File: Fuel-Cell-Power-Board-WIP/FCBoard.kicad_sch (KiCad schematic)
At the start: 99 parts, among them J1 STD_PWR_HEADER, J2 DE9_Receptacle, J3 STD_PWR_HEADER, J4 STD_PWR_HEADER, J5 Conn_02x05_Odd_Even, J6 STD_PWR_HEADER, J7 DA15_Receptacle_MountingHoles, J7 USB_B_Micro, Q1 NMOS, SW1 PTS815 SJM 250 SMTR LFS, SW2 PTS815 SJM 250 SMTR LFS, U2 LM2576D2TR4-5G, U3 RPA60-2412SFW, U3 TPS2596, U4 STM32L432KCUx, U6 FT234XD-R, U7 LD39050PU33R, U9 MCP2542FD-E/SN, U9 USBLC6-2SC6, X1 OXETDLJANF-8MHZ

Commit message: Began PCB layout.
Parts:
- C4: footprint (none) -> FPCB_Footprints:PCAP_10x10-ELECT_NCA
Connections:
- net +12V is gone; now on net 12V_{FC}: C1.1, U2.1 (VIN)
- net I_{MON}: no longer R9.1, U3.7 (ILM)
- net ~{FAULT}: no longer Q1.2 (G), R10.2, U3.6 (~{FAULT})
- new net I_{MON}12V: R9.1, U3.7 (ILM)
- new net ~{FAULT}12V: Q1.2 (G), R10.2, U3.6 (~{FAULT})
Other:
- note added: "Fuel Cell Power In and 12V DCDC"
- moved on the sheet: J3, J4

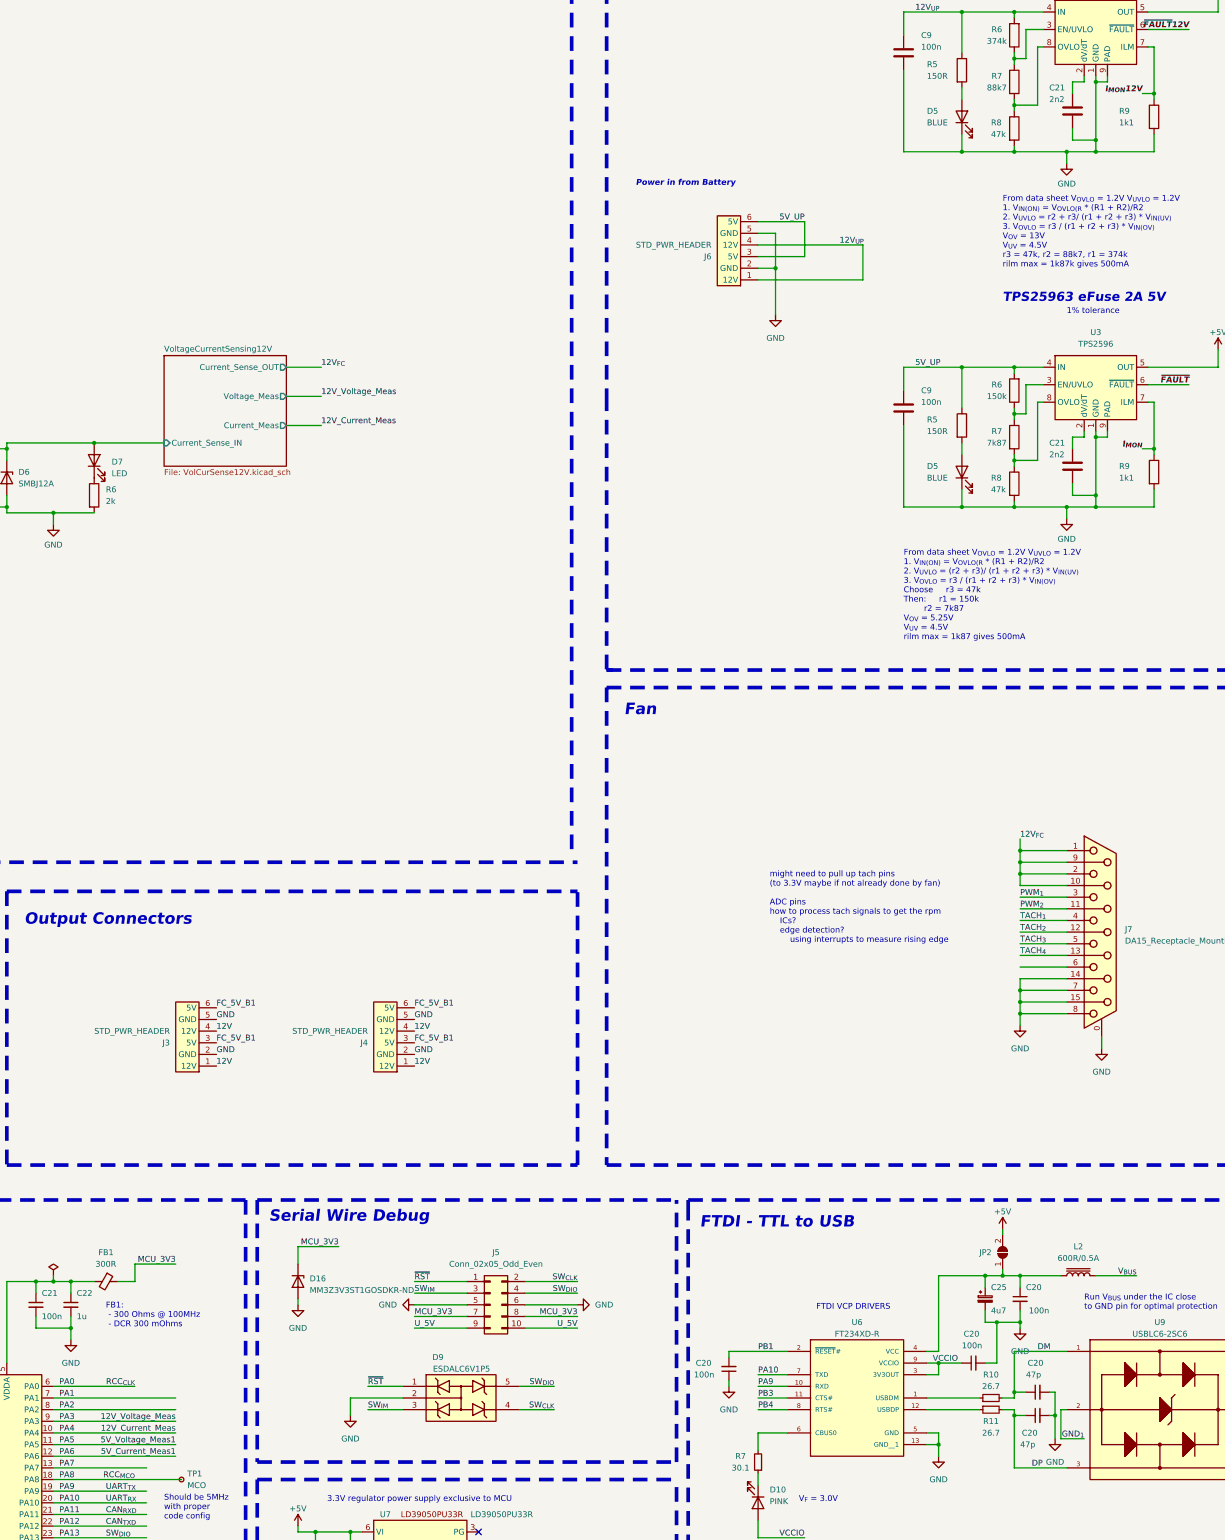
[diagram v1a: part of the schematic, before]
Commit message: Routed PCB except for battery 5V
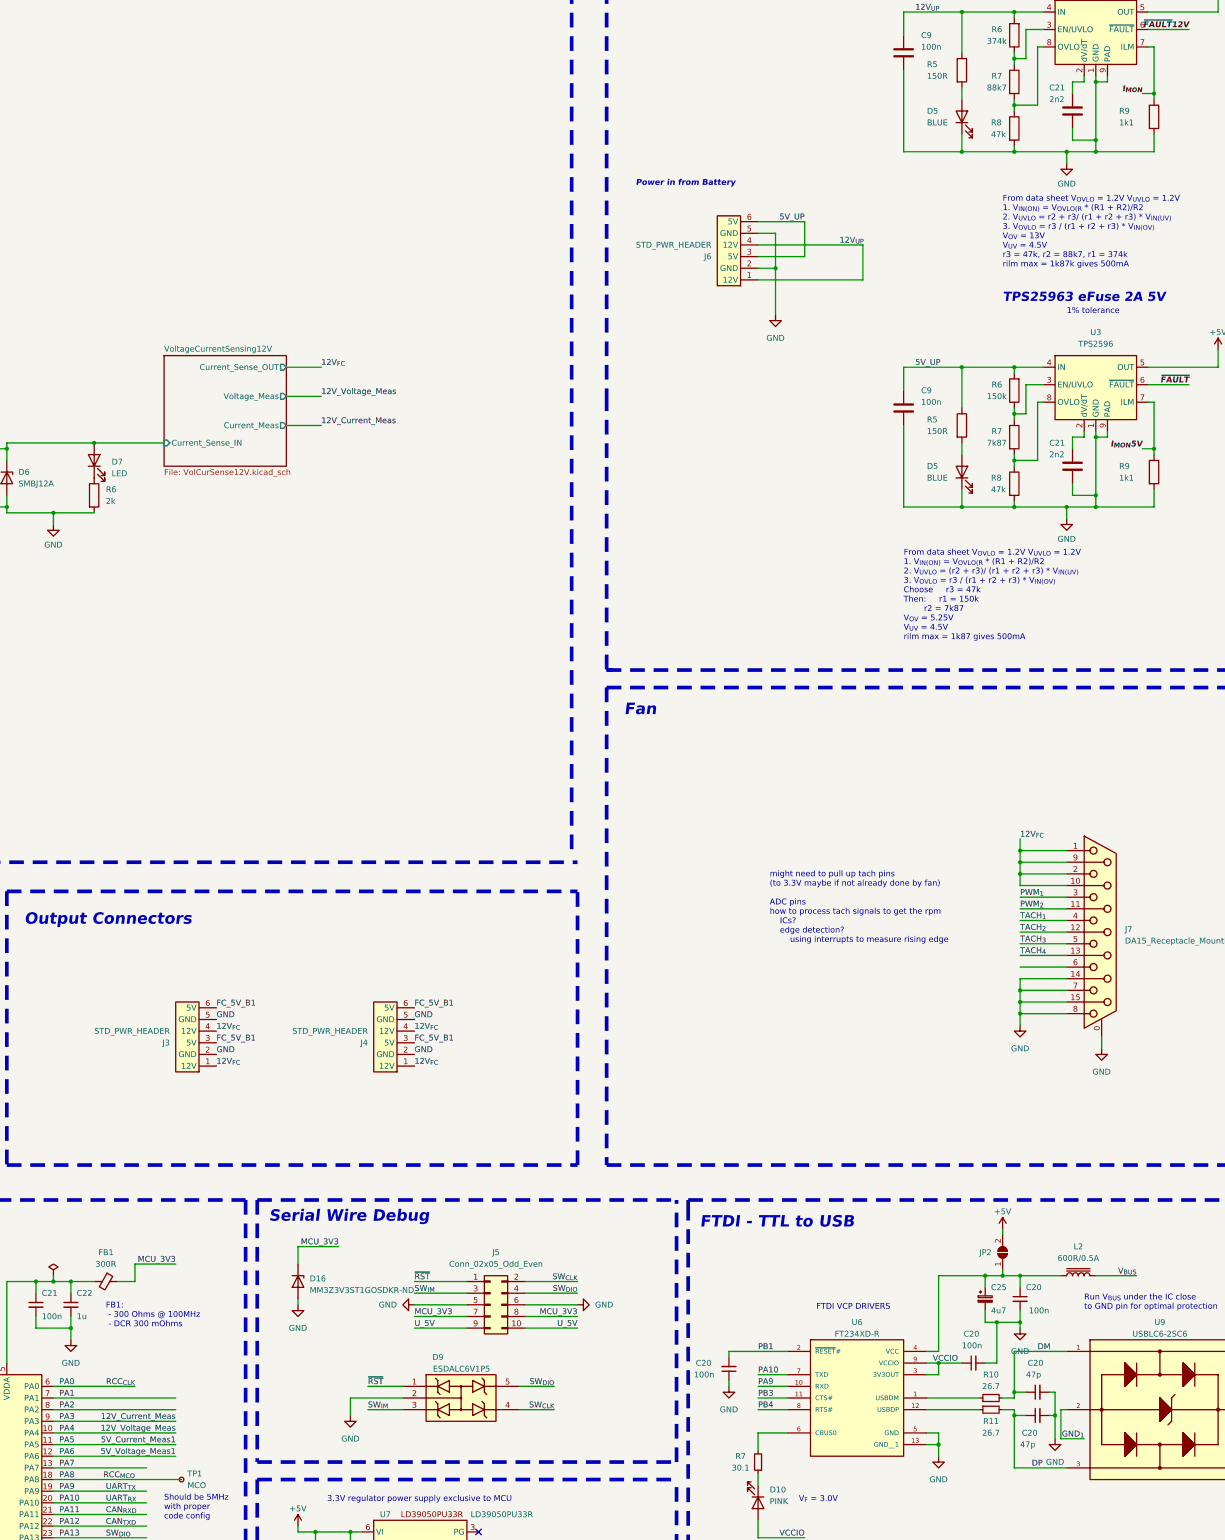
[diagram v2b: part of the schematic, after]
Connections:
- net 12V is gone; now on net 12V_{FC}: J3.1 (12V), J3.4 (12V), J4.1 (12V), J4.4 (12V)
- net I_{MON}12V is gone; now on net I_{MON}: R9.1, U3.7 (ILM)
- net 12V_Current_Meas: now also U4.9 (PA3); no longer U4.10 (PA4)
- net 12V_Voltage_Meas: now also U4.10 (PA4); no longer U4.9 (PA3)
- net 5V_Current_Meas1: now also U4.11 (PA5); no longer U4.12 (PA6)
- net 5V_Voltage_Meas1: now also U4.12 (PA6); no longer U4.11 (PA5)
- net I_{MON}: no longer R9.1, U3.7 (ILM)
- new net I_{MON}5V: R9.1, U3.7 (ILM)
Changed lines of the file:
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@@
-    (effects (font (size 1.27 1.27)) (justify left bottom))
-  )
-  (label "12V" (at 303.53 267.97 0) (fields_autoplaced)
     (effects (font (size 1.27 1.27)) (justify left bottom))
   )
@@
     (effects (font (size 1.27 1.27)) (justify left bottom))
   )
+  (label "12V_{FC}" (at 303.53 267.97 0) (fields_autoplaced)
+    (effects (font (size 1.27 1.27)) (justify left bottom))
+  )
   (label "~{FAULT}12V" (at 535.94 68.58 180) (fields_autoplaced)
     (effects (font (size 1.27 1.27) bold italic) (justify right bottom))
@@
     (effects (font (size 1.27 1.27) bold italic) (justify right bottom))
   )
-  (label "12V_Current_Meas" (at 294.64 347.98 180) (fields_autoplaced)
-    (effects (font (size 1.27 1.27)) (justify right bottom))
+  (label "5V_Current_Meas1" (at 294.64 350.52 180) (fields_autoplaced)
+    (effects (font (size 1.27 1.27)) (justify right bottom))
+  )
+  (label "12V_{FC}" (at 346.71 260.35 0) (fields_autoplaced)
+    (effects (font (size 1.27 1.27)) (justify left bottom))
   )
   (label "12V_{FC}" (at 326.39 115.57 0) (fields_autoplaced)
@@
     (effects (font (size 1.27 1.27)) (justify left bottom))
   )
-  (label "12V" (at 346.71 267.97 0) (fields_autoplaced)
-    (effects (font (size 1.27 1.27)) (justify left bottom))
-  )
   (label "PA11" (at 269.24 365.76 0) (fields_autoplaced)
     (effects (font (size 1.27 1.27)) (justify left bottom))
@@
     (effects (font (size 1.27 1.27)) (justify left bottom))
   )
-  (label "12V" (at 303.53 260.35 0) (fields_autoplaced)
-    (effects (font (size 1.27 1.27)) (justify left bottom))
-  )
   (label "V_{BUS}" (at 504.19 313.69 180) (fields_autoplaced)
     (effects (font (size 1.27 1.27)) (justify right bottom))
@@
     (effects (font (size 1.27 1.27)) (justify left bottom))
   )
-  (label "12V_Voltage_Meas" (at 294.64 345.44 180) (fields_autoplaced)
-    (effects (font (size 1.27 1.27)) (justify right bottom))
-  )
   (label "PB3" (at 237.49 360.68 0) (fields_autoplaced)
     (effects (font (size 1.27 1.27)) (justify left bottom))
@@
     (effects (font (size 1.27 1.27)) (justify left bottom))
   )
-  (label "12V" (at 346.71 260.35 0) (fields_autoplaced)
-    (effects (font (size 1.27 1.27)) (justify left bottom))
+  (label "12V_Current_Meas" (at 294.64 345.44 180) (fields_autoplaced)
+    (effects (font (size 1.27 1.27)) (justify right bottom))
   )
   (label "SW_{IM}" (at 346.71 317.5 0) (fields_autoplaced)
@@
     (effects (font (size 1.27 1.27)) (justify right bottom))
   )
-  (label "5V_Voltage_Meas1" (at 294.64 350.52 180) (fields_autoplaced)
-    (effects (font (size 1.27 1.27)) (justify right bottom))
-  )
   (label "12V_{FC}" (at 30.48 252.73 0) (fields_autoplaced)
     (effects (font (size 1.27 1.27)) (justify left bottom))
@@
     (effects (font (size 1.27 1.27)) (justify left bottom))
   )
+  (label "5V_Voltage_Meas1" (at 294.64 353.06 180) (fields_autoplaced)
+    (effects (font (size 1.27 1.27)) (justify right bottom))
+  )
   (label "U_5V" (at 346.71 325.12 0) (fields_autoplaced)
     (effects (font (size 1.27 1.27)) (justify left bottom))
@@
     (effects (font (size 1.27 1.27)) (justify left bottom))
   )
-  (label "5V_Current_Meas1" (at 294.64 353.06 180) (fields_autoplaced)
-    (effects (font (size 1.27 1.27)) (justify right bottom))
-  )
   (label "PB0" (at 237.49 355.6 0) (fields_autoplaced)
     (effects (font (size 1.27 1.27)) (justify left bottom))
@@
     (effects (font (size 1.27 1.27)) (justify left bottom))
   )
-  (label "I_{MON}12V" (at 505.46 55.88 180) (fields_autoplaced)
+  (label "I_{MON}" (at 505.46 55.88 180) (fields_autoplaced)
     (effects (font (size 1.27 1.27) bold italic) (justify right bottom))
   )
@@
     (effects (font (size 1.27 1.27)) (justify left bottom))
   )
-  (label "I_{MON}" (at 505.46 133.35 180) (fields_autoplaced)
+  (label "I_{MON}5V" (at 505.46 133.35 180) (fields_autoplaced)
     (effects (font (size 1.27 1.27) bold italic) (justify right bottom))
   )
@@
     (effects (font (size 1.27 1.27)) (justify left bottom))
   )
+  (label "12V_Voltage_Meas" (at 294.64 347.98 180) (fields_autoplaced)
+    (effects (font (size 1.27 1.27)) (justify right bottom))
+  )
   (label "GND" (at 303.53 265.43 0) (fields_autoplaced)
     (effects (font (size 1.27 1.27)) (justify left bottom))
@@
     (effects (font (size 1.27 1.27)) (justify left bottom))
   )
+  (label "12V_{FC}" (at 346.71 267.97 0) (fields_autoplaced)
+    (effects (font (size 1.27 1.27)) (justify left bottom))
+  )
   (label "GND_{1}" (at 554.99 353.06 0) (fields_autoplaced)
     (effects (font (size 1.27 1.27)) (justify left bottom))
@@
     (effects (font (size 1.27 1.27)) (justify left bottom))
   )
+  (label "12V_{FC}" (at 303.53 260.35 0) (fields_autoplaced)
+    (effects (font (size 1.27 1.27)) (justify left bottom))
+  )

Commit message: moved james pcb to another folder so we can do rev 2 of the layout, changed some footprints to be consistent with kicad, changed the inductor to a smaller bit similar package with certain characteristics
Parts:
- removed C11: 100u, FPCB_Footprints:CAP_UAQ_12P5X20_NCH, symbol Device:C_Polarized
- added C12: 100u, Capacitor_THT:CP_Radial_D12.5mm_P5.00mm, symbol Device:C_Polarized
- added L1: 100u, FPCB_Footprints:IND_101M51_VIS, symbol Device:L
- C4: footprint FPCB_Footprints:PCAP_10x10-ELECT_NCA -> Capacitor_SMD:CP_Elec_10x10
- C5: footprint FPCB_Footprints:CAP_UAQ_12P5X20_NCH -> Capacitor_THT:CP_Radial_D12.5mm_P5.00mm
- L2: renamed from L1; footprint FPCB_Footprints:IND_101M51_VIS -> Inductor_SMD:L_Vishay_IHLP-6767; Name IHLP8787MZER101M51 -> 541-1294-1-ND
- R2: value 3.1k -> 0R
- R3: now not fitted
- renumbered C6 to C8, D2 to D1, D1 to D2, L2 to L3
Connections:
- net GND: now also C12.2
- net VoltageCurrentSensing12V/Current_Sense_IN: now also C12.1

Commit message: updated schematic slightly
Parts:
- added C22: 1u, Capacitor_SMD:C_0603_1608Metric, symbol Device:C_Small
- added R10 (x2): 10k, Resistor_SMD:R_0603_1608Metric, symbol Device:R
- added U14: TSV912IDT, symbol Amplifier_Operational:TSV912IDT
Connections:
- net TACH_{1} is gone; now on net PA1: J7.4
- net TACH_{2} is gone; now on net PA2: J7.12 (P12)
- net +5V: now also C22.1, U14.8 (V+)
- net GND: now also C22.2, U14.4 (V-)
- net MCU_3V3: now also R10.1, R10.1
- net PA1: now also R10.2
- net PA2: now also R10.2
- net PB5: now also U14.3 (+)
- net PB6: now also U14.5 (+)
- net PWM_{1}: no longer names the net of J7.3
- net PWM_{1}: now also U14.1, U14.2 (-)
- net PWM_{2}: no longer names the net of J7.11 (P111)
- net PWM_{2}: now also U14.6 (-), U14.7
- no-connect marks 8 -> 20
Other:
- note added: "Positive pull up logic for CTRL pin, open circuit is on"
- moved on the sheet: J7

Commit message: started rework
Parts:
- removed C21: 2n2, Capacitor_SMD:C_0603_1608Metric, symbol Device:C
- removed C9: 100n, Capacitor_SMD:C_0603_1608Metric, symbol Device:C
- removed D5: BLUE, LED_SMD:LED_0603_1608Metric, symbol Device:LED
- removed D6: RED, LED_SMD:LED_0603_1608Metric, symbol Device:LED
- removed Q1 (x2): NMOS, Package_TO_SOT_SMD:SOT-523, symbol Simulation_SPICE:NMOS
- removed R10: 10k, Resistor_SMD:R_0603_1608Metric, symbol Device:R
- removed R11: 120R, Resistor_SMD:R_0603_1608Metric, symbol Device:R
- removed R5: 150R, Resistor_SMD:R_0603_1608Metric, symbol Device:R
- removed R6: 374k, Resistor_SMD:R_0603_1608Metric, symbol Device:R
- removed R7: 88k7, Resistor_SMD:R_0603_1608Metric, symbol Device:R
- removed R8: 47k, Resistor_SMD:R_0603_1608Metric, symbol Device:R
- removed R9: 1k1, Resistor_SMD:R_0603_1608Metric, symbol Device:R
- removed U3: TPS2596, Package_SO:TI_SO-PowerPAD-8, symbol H2_Parts:TPS2596
- added H1, H2, H3, H4: MountingHole, MountingHole:MountingHole_3.2mm_M3, symbol Mechanical:MountingHole
- added Q1: SI2302A-TPMSCT-ND, Package_TO_SOT_SMD:SOT-23-3, symbol Device:Q_NMOS_GSD
- C10, C9: footprint Capacitor_SMD:C_1812_4532Metric -> Capacitor_SMD:C_2220_5650Metric; Part 1812GC682KAT1A -> 478-5929-2-ND
- C22: value 1u -> 100n
- U7: renamed from U14; footprint (none) -> BATT_FTP:SO8_STM
- renumbered C25 to C24, R10 to R11, R11 to R12
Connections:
- net GND: now also Q1.2 (S)
- net ~{FAULT}: now also Q1.1 (G)
- net at D6.1 (K): now also Q1.3 (D)
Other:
- note removed: "From data sheet V_{OVLO} = 1.2V V_{UVLO} = 1.2V 1. V_{IN(ON)} = V_{OVLO(R} * (R1 + R2)/R2 2. V_{UVLO} = r2 + r3/ (r1 + r2 + r3) * V_{IN(UV)} 3. V_{OVLO} = r3 / (r1 + r2 + r3) * V_{IN(OV)} V_{OV} = 13V V_{UV} = 4.5V r3 = 47k, r2 = 88k7, r1 = 374k rilm max = 1k87k gives 500mA"
- note removed: "TPS25963 eFuse 2A 12V"

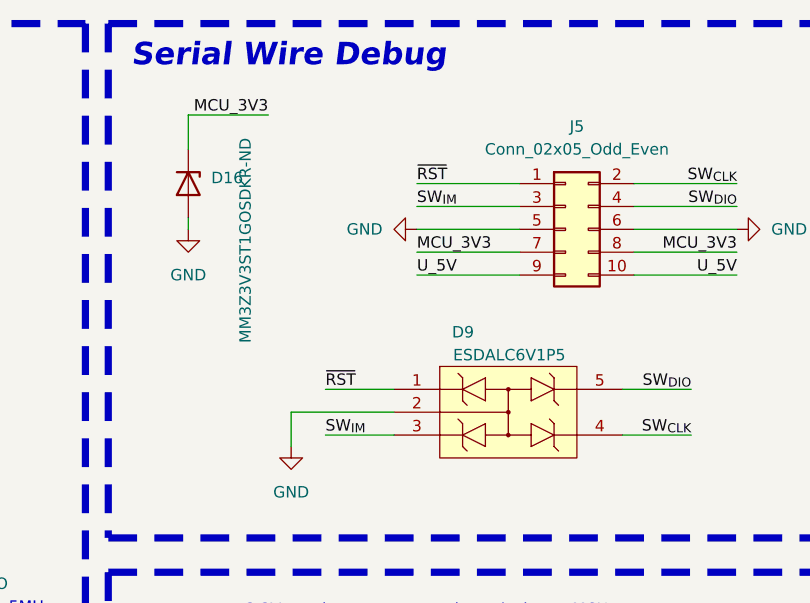
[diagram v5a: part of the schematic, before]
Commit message: Reworked mcu layout for caps, reworked ftdi chip layout, reworked lots of other things too
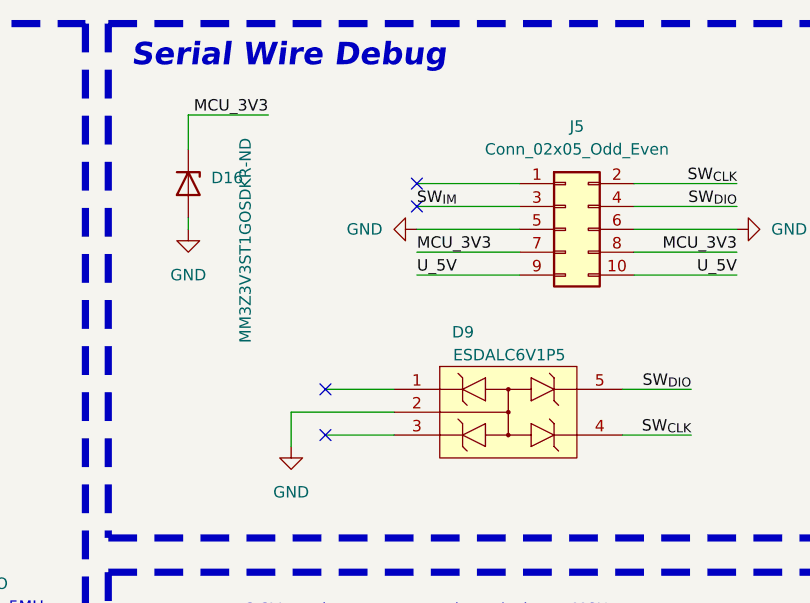
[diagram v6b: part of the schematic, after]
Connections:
- net SW_{IM}: no longer D9.3
- net ~{RST}: no longer D9.1, J5.1 (Pin_1)
- no-connect marks 20 -> 24
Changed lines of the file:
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@@
   (no_connect (at 505.46 245.11))
   (no_connect (at 226.06 138.43))
+  (no_connect (at 346.71 314.96))
   (no_connect (at 86.36 345.44))
+  (no_connect (at 336.55 337.82))
   (no_connect (at 109.22 332.74))
   (no_connect (at 505.46 250.19))
   (no_connect (at 86.36 337.82))
+  (no_connect (at 346.71 317.5))
+  (no_connect (at 336.55 342.9))
   (no_connect (at 237.49 350.52))
   (no_connect (at 86.36 330.2))
@@
     (effects (font (size 1.27 1.27)) (justify right bottom))
   )
-  (label "~{RST}" (at 336.55 337.82 0) (fields_autoplaced)
-    (effects (font (size 1.27 1.27)) (justify left bottom))
-  )
   (label "TACH_{2}" (at 505.46 242.57 0) (fields_autoplaced)
     (effects (font (size 1.27 1.27)) (justify left bottom))
@@
     (effects (font (size 1.27 1.27)) (justify left bottom))
   )
-  (label "SW_{IM}" (at 336.55 342.9 0) (fields_autoplaced)
-    (effects (font (size 1.27 1.27)) (justify left bottom))
-  )
   (label "V+" (at 101.6 330.2 0) (fields_autoplaced)
     (effects (font (size 1.27 1.27)) (justify left bottom))
@@
     (effects (font (size 1.27 1.27)) (justify left bottom))
   )
-  (label "~{RST}" (at 346.71 314.96 0) (fields_autoplaced)
-    (effects (font (size 1.27 1.27)) (justify left bottom))
-  )

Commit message: finished up pcb
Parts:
- removed L1: 100u, FPCB_Footprints:IND_101M51_VIS, symbol Device:L
- added JP3: SolderJumper_3_Open, Jumper:SolderJumper-3_P1.3mm_Open_RoundedPad1.0x1.5mm_NumberLabels, symbol Jumper:SolderJumper_3_Open
- added Q2, Q3: SI2302A-TPMSCT-ND, Package_TO_SOT_SMD:SOT-23-3, symbol Device:Q_NMOS_GSD
- added R10 (x2): 10k, Resistor_SMD:R_0603_1608Metric, symbol Device:R
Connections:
- net 12V_{FC}: now also JP3.1 (A)
- net GND: now also Q2.2 (S), Q3.2 (S)
- net MCU_3V3: now also JP3.3 (B)
- net at U7.1, U7.2 (-): now also Q3.1 (G); no longer J7.3
- net at U7.6 (-), U7.7: now also Q2.1 (G); no longer J7.11 (P111)
- new net: JP3.2 (C), R10.2, R10.2
- new net PWM_{1,Buff}: J7.3, Q3.3 (D), R10.1
- new net PWM_{2,Buff}: J7.11 (P111), Q2.3 (D), R10.1
- no-connect marks 24 -> 22
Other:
- note removed: "might need to pull up tach pins (to 3.3V maybe if not already done by fan) ADC pins how to process tach signals to get the rpm ICs? edge detection? using interrupts to measure rising edge"
- moved on the sheet: R10, U7A, U7B
